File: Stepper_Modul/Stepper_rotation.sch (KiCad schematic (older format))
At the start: 14 parts, among them SW201 SW_DIP_x03, U201 TMC2226

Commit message: motor controller von stepper-treibern getrennt, sodass es modular ist. Libraries werden nun übergreifend von allen projekten verwendet
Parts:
- removed C201, C205, C206, C207: 100n 50V, Capacitor_SMD:C_0603_1608Metric, symbol Device:C_Small
- removed C202, C203: 2.2u 50V, Capacitor_SMD:C_1210_3225Metric, symbol Device:C_Small
- removed C204: 22n 50V, Capacitor_SMD:C_0603_1608Metric, symbol Device:C_Small
- removed C208, C209: 100u 35V, Capacitor_THT:CP_Radial_D6.3mm_P2.50mm, symbol Device:CP_Small
- removed R201: 22k, Resistor_SMD:R_0603_1608Metric, symbol Device:R_Small
- removed R202, R203: 0.22R 0.5W, Resistor_SMD:R_1210_3225Metric, symbol Device:R_Small
- removed SW201: SW_DIP_x03, Package_DIP:DIP-6_W7.62mm, symbol Switch:SW_DIP_x03
- removed U201: TMC2226, Package_SO:TSSOP-28-1EP_4.4x9.7mm_P0.65mm, symbol StepperBoard-rescue:TMC2226-Pick_n_Place
- added C501, C505, C506, C507: 100n 50V, Capacitor_SMD:C_0603_1608Metric, symbol Device:C_Small
- added C502, C503: 2.2u 50V, Capacitor_SMD:C_1210_3225Metric, symbol Device:C_Small
- added C504: 22n 50V, Capacitor_SMD:C_0603_1608Metric, symbol Device:C_Small
- added C508, C509: 100u 35V, Capacitor_THT:CP_Radial_D6.3mm_P2.50mm, symbol Device:CP_Small
- added R501: 22k, Resistor_SMD:R_0603_1608Metric, symbol Device:R_Small
- added R502, R503: 0.1R 0.5W, Resistor_SMD:R_1210_3225Metric, symbol Device:R_Small
- added SW501: SW_DIP_x03, Package_DIP:DIP-6_W7.62mm, symbol Switch:SW_DIP_x03
- added U501: TMC2226, Package_SO:TSSOP-28-1EP_4.4x9.7mm_P0.65mm, symbol PorjectLibrary:TMC2226
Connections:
- net +24V: now also C505.2, C506.2, C507.2, C508.1, C509.1, U501.26 (VS), U501.3 (VS)
- net +3V3: now also C501.2, SW501.1, SW501.2, SW501.3, U501.19 (VCC_IO)
- net 5VOUT: now also C502.2, U501.11 (5VOUT)
- net GND: now also C501.1, C502.1, C503.1, C506.1, C507.1, C508.2, C509.2, R502.1, R503.1, U501.17 (CLK), U501.22 (GND), U501.24 (STDBY), U501.29 (GND), U501.6 (GND)
- net SINGLE_WIRE: now also U501.18 (PND_UART)
- new net: C505.1, U501.9 (VCP)
- new net: SW501.4, U501.10 (SPREAD)
- new net: SW501.6, U501.12 (MS1_AD0)
- new net: SW501.5, U501.14 (MS2_AD1)
- new net: R503.2, U501.2 (BRB)
- new net: C503.2, R501.1, U501.21 (VREF)
- new net: R502.2, U501.27 (BRA)
- new net: C504.2, U501.7 (CPO)
- new net: C504.1, U501.8 (CPI)
- new net CUR_CONTROL_ROT: R501.2
- new net DIAG_ROT: U501.15 (DIAG)
- new net DIR_ROT: U501.23 (DIR)
- new net EN_ROT: U501.5 (ENN)
- new net INDEX_ROT: U501.16 (INDEX)
- new net OA1_ROT: U501.28 (OA1)
- new net OA2_ROT: U501.25 (OA2)
- new net OB1_ROT: U501.1 (OB1)
- new net OB2_ROT: U501.4 (OB2)
- new net STEP_ROT: U501.20 (STEP)
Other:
- note added: "1920mA"
- note removed: "100mOhm C270892"
- note removed: "960mA"

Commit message: stepper board fertig gestellt
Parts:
- R501: value 22k -> 22K1; LCSC C31850 -> C137768
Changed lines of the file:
@@
 AR Path="/5FCB2242/5FCB624A" Ref="R501"  Part="1"
 F 0 "R501" V 5114 950 50  0000 C CNN
-F 1 "22k" V 5205 950 50  0000 C CNN
+F 1 "22K1" V 5205 950 50  0000 C CNN
 F 2 "Resistor_SMD:R_0603_1608Metric" H 5400 950 50  0001 C CNN
 F 3 "~" H 5400 950 50  0001 C CNN
-F 4 "C31850" V 5296 950 50  0000 C CNN "LCSC"
+F 4 "C137768" V 5296 950 50  0000 C CNN "LCSC"
 	1    5400 950
 	0    1    1    0

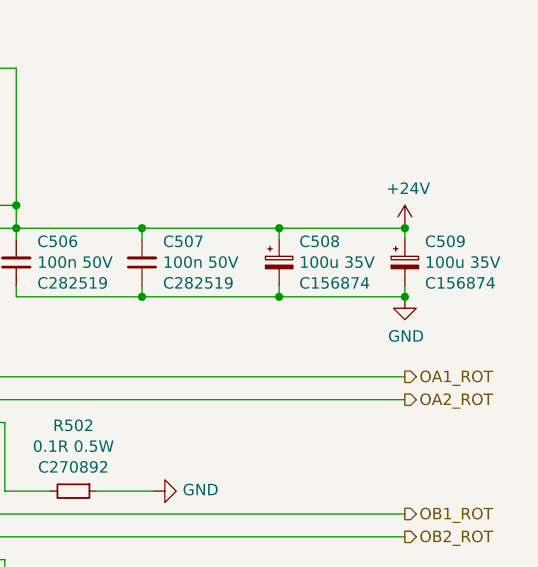
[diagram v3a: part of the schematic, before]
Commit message: BOM für LCSC überarbeitet. Tool für BOM export modifiziert
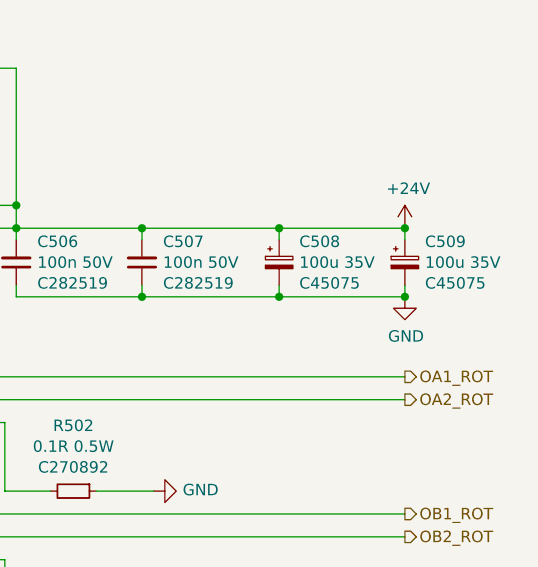
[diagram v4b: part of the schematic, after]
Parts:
- C508, C509: LCSC C156874 -> C45075
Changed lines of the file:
@@
 F 2 "Capacitor_THT:CP_Radial_D6.3mm_P2.50mm" H 8900 2200 50  0001 C CNN
 F 3 "https://datasheet.lcsc.com/szlcsc/Guangdong-TOPAZ-Elec-Tech-ECSS0608101M035P00_C156874.pdf" H 8900 2200 50  0001 C CNN
-F 4 "C156874" H 8988 2109 50  0000 L CNN "LCSC"
+F 4 "C45075" H 8988 2109 50  0000 L CNN "LCSC"
 	1    8900 2200
 	1    0    0    -1
@@
 F 2 "Capacitor_THT:CP_Radial_D6.3mm_P2.50mm" H 9450 2200 50  0001 C CNN
 F 3 "https://datasheet.lcsc.com/szlcsc/Guangdong-TOPAZ-Elec-Tech-ECSS0608101M035P00_C156874.pdf" H 9450 2200 50  0001 C CNN
-F 4 "C156874" H 9538 2109 50  0000 L CNN "LCSC"
+F 4 "C45075" H 9538 2109 50  0000 L CNN "LCSC"
 	1    9450 2200
 	1    0    0    -1

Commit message: Änderungen für bestellung V01 -  Bestellung abgeschickt
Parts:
- R502, R503: value 0.1R 0.5W -> 1R 0.5W; LCSC C270892 -> C136108
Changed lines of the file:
@@
 AR Path="/5FCB2242/5FCB6235" Ref="R502"  Part="1"
 F 0 "R502" V 7714 3200 50  0000 C CNN
-F 1 "0.1R 0.5W" V 7805 3200 50  0000 C CNN
+F 1 "1R 0.5W" V 7805 3200 50  0000 C CNN
 F 2 "Resistor_SMD:R_1210_3225Metric" H 8000 3200 50  0001 C CNN
 F 3 "~" H 8000 3200 50  0001 C CNN
-F 4 "C270892" V 7896 3200 50  0000 C CNN "LCSC"
+F 4 "C136108" V 7896 3200 50  0000 C CNN "LCSC"
 	1    8000 3200
 	0    1    1    0
@@
 AR Path="/5FCB2242/5FCB6239" Ref="R503"  Part="1"
 F 0 "R503" V 7714 3850 50  0000 C CNN
-F 1 "0.1R 0.5W" V 7805 3850 50  0000 C CNN
+F 1 "1R 0.5W" V 7805 3850 50  0000 C CNN
 F 2 "Resistor_SMD:R_1210_3225Metric" H 8000 3850 50  0001 C CNN
 F 3 "~" H 8000 3850 50  0001 C CNN
-F 4 "C270892" V 7896 3850 50  0000 C CNN "LCSC"
+F 4 "C136108" V 7896 3850 50  0000 C CNN "LCSC"
 	1    8000 3850
 	0    1    1    0
